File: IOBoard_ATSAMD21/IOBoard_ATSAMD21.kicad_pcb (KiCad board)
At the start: 2 copper layers, 76.2 x 128.5 mm, 36 parts, among them J1 Conn_PIC_ICSP_ICD, J2 Conn_01x04_Male, SW1 EG_1218, SW2 EG_1218, SW3 EG_1218, SW4 EG_1218, U1 ATSAMD21G18A-A, U2 AP2112K-3.3

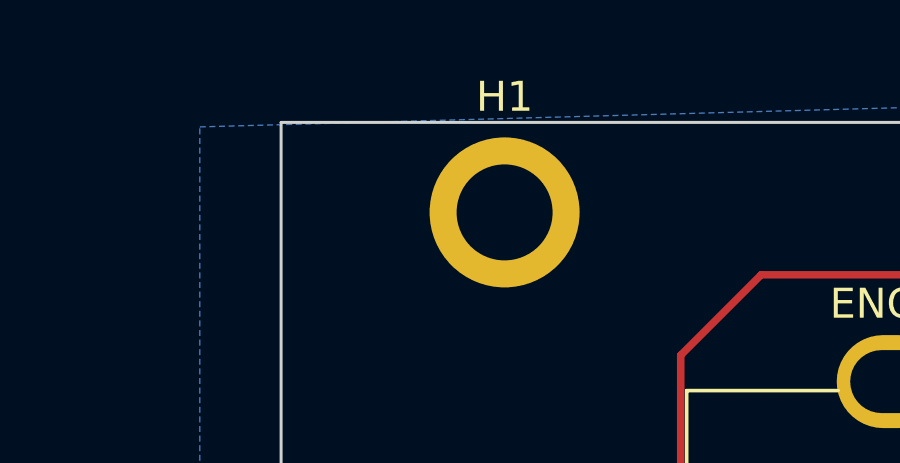
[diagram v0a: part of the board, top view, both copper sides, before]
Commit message: added dimensions to f.fab layer
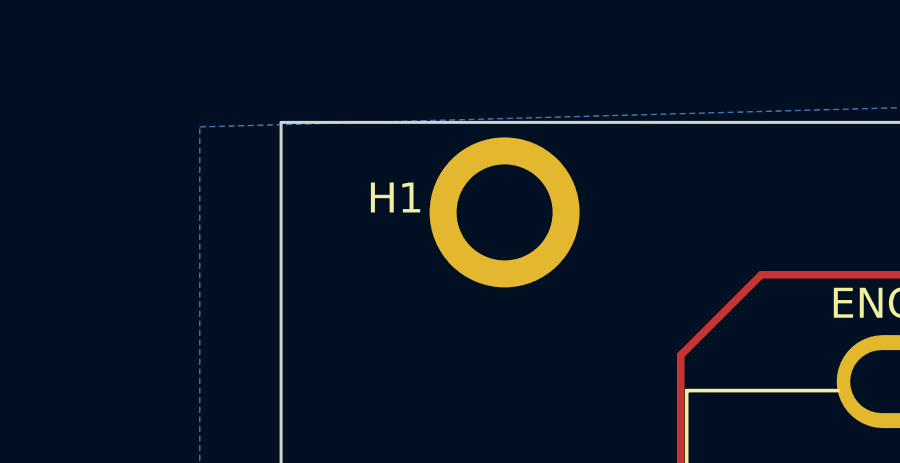
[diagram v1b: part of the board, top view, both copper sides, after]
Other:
- board text added: "0.6in"
- board text added: "0.8in"
- board text added: "1.4in"
- board text added: "1in"
- board text added: "3mm"
- board text added: "7.45mm"
- board text added: "Board Height: 128.5mm/5.06in"
- board text added: "Board Width: 76.2mm/3in/15HP"
- board text added: "Distance from left to right holes: 60.96mm/2.6in/13HP"
- board text added: "LEDs from top: 4.35in"
- board text added: "Switches from top: 3.6in"
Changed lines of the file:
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@@
     )
     (pad_to_mask_clearance 0)
-    (grid_origin 57.45 50)
+    (grid_origin 50 50)
     (pcbplotparams
       (layerselection 0x00010fc_ffffffff)
@@
       (effects (font (size 1 1) (thickness 0.15)))
     )
-    (fp_text value "RotaryEncoder_Switch" (at 1.92 11.12 180 unlocked) (layer "F.Fab")
+    (fp_text value "RotaryEncoder_Switch" (at -0.46 -10.16 unlocked) (layer "F.Fab")
       (effects (font (size 1 1) (thickness 0.15)))
     )
     (fp_text user "${REFERENCE}" (at -0.36 0 270) (layer "F.Fab")
-      (effects (font (size 1 1) (thickness 0.15)))
-    )
-    (fp_text user "${REFERENCE}" (at 1.46 12.62 180 unlocked) (layer "F.Fab")
       (effects (font (size 1 1) (thickness 0.15)))
     )
@@
     (property "Sheetname" "")
     (attr exclude_from_pos_files)
-    (fp_text reference "H1" (at 0 -3.85) (layer "F.SilkS")
+    (fp_text reference "H1" (at -3.64 -0.46) (layer "F.SilkS")
       (effects (font (size 1 1) (thickness 0.15)))
     )
@@
   )
   (gr_rect (start 50 50) (end 126.2 178.5) (layer "Edge.Cuts") (width 0.1) (fill none))
+  (gr_line (start 126.2 43.65) (end 126.2 42.38) (layer "B.Fab") (width 0.1))
+  (gr_line (start 136.36 178.27) (end 135.09 178.27) (layer "B.Fab") (width 0.1))
+  (gr_line (start 137.63 50) (end 136.36 50) (layer "B.Fab") (width 0.1))
+  (gr_line (start 50 43.65) (end 50 42.38) (layer "B.Fab") (width 0.1))
+  (gr_line (start 95.72 160.49) (end 110.96 160.49) (layer "F.Fab") (width 0.1))
+  (gr_line (start 118.58 47.46) (end 118.58 46.19) (layer "F.Fab") (width 0.1))
+  (gr_line (start 118.58 46.19) (end 118.58 47.46) (layer "F.Fab") (width 0.1))
+  (gr_line (start 70.32 65.24) (end 50 65.24) (layer "F.Fab") (width 0.1))
+  (gr_line (start 114.77 160.49) (end 110.96 160.49) (layer "F.Fab") (width 0.1))
+  (gr_line (start 110.96 160.49) (end 126.2 160.49) (layer "F.Fab") (width 0.1))
+  (gr_line (start 70.32 90.64) (end 71.59 90.64) (layer "F.Fab") (width 0.1))
+  (gr_line (start 65.24 141.44) (end 50 141.44) (layer "F.Fab") (width 0.1))
+  (gr_line (start 50 46.19) (end 50 47.46) (layer "F.Fab") (width 0.1))
+  (gr_line (start 46 50) (end 47 50) (layer "F.Fab") (width 0.1))
+  (gr_line (start 135.09 178.27) (end 137.63 178.27) (layer "F.Fab") (width 0.1))
+  (gr_line (start 57.62 47.46) (end 57.62 48.73) (layer "F.Fab") (width 0.1))
+  (gr_line (start 80.48 160.49) (end 95.72 160.49) (layer "F.Fab") (width 0.1))
+  (gr_line (start 132.55 50) (end 132.55 160.49) (layer "F.Fab") (width 0.1))
+  (gr_line (start 110.96 141.44) (end 95.72 141.44) (layer "F.Fab") (width 0.1))
+  (gr_line (start 46 53) (end 48 53) (layer "F.Fab") (width 0.1))
+  (gr_line (start 47 50) (end 47 53) (layer "F.Fab") (width 0.1))
+  (gr_line (start 118.58 47.46) (end 57.62 47.46) (layer "F.Fab") (width 0.1))
+  (gr_line (start 130.01 141.44) (end 127.47 141.44) (layer "F.Fab") (width 0.1))
+  (gr_line (start 105.88 50) (end 105.88 65.24) (layer "F.Fab") (width 0.1))
+  (gr_line (start 70.32 90.64) (end 69.05 90.64) (layer "F.Fab") (width 0.1))
+  (gr_line (start 50 43.65) (end 126.2 43.65) (layer "F.Fab") (width 0.1))
+  (gr_line (start 131.28 160.49) (end 133.82 160.49) (layer "F.Fab") (width 0.1))
+  (gr_line (start 70.32 65.24) (end 70.32 66.51) (layer "F.Fab") (width 0.1))
+  (gr_line (start 50 48.73) (end 50 47.46) (layer "F.Fab") (width 0.1))
+  (gr_line (start 70.32 65.24) (end 70.32 63.97) (layer "F.Fab") (width 0.1))
+  (gr_line (start 127.47 141.44) (end 128.74 141.44) (layer "F.Fab") (width 0.1))
+  (gr_line (start 95.72 141.44) (end 110.96 141.44) (layer "F.Fab") (width 0.1))
+  (gr_line (start 132.55 160.49) (end 131.28 160.49) (layer "F.Fab") (width 0.1))
+  (gr_line (start 105.88 65.24) (end 70.32 65.24) (layer "F.Fab") (width 0.1))
+  (gr_line (start 48 50) (end 46 50) (layer "F.Fab") (width 0.1))
+  (gr_line (start 65.24 141.44) (end 80.48 141.44) (layer "F.Fab") (width 0.1))
+  (gr_line (start 65.24 160.61) (end 80.48 160.49) (layer "F.Fab") (width 0.1))
+  (gr_line (start 80.48 141.44) (end 95.72 141.44) (layer "F.Fab") (width 0.1))
+  (gr_line (start 110.96 141.44) (end 126.2 141.44) (layer "F.Fab") (width 0.1))
+  (gr_line (start 48 53) (end 47 53) (layer "F.Fab") (width 0.1))
+  (gr_line (start 70.32 63.97) (end 70.32 65.24) (layer "F.Fab") (width 0.1))
+  (gr_line (start 118.58 48.73) (end 118.58 47.46) (layer "F.Fab") (width 0.1))
+  (gr_line (start 127.47 50) (end 130.01 50) (layer "F.Fab") (width 0.1))
+  (gr_line (start 70.32 90.64) (end 70.32 65.24) (layer "F.Fab") (width 0.1))
+  (gr_line locked (start 128.74 141.44) (end 128.74 50) (layer "F.Fab") (width 0.1))
+  (gr_line (start 126.2 42.38) (end 126.2 44.92) (layer "F.Fab") (width 0.1))
+  (gr_line (start 133.82 50) (end 131.28 50) (layer "F.Fab") (width 0.1))
+  (gr_line (start 57.62 47.46) (end 50 47.46) (layer "F.Fab") (width 0.1))
+  (gr_line (start 57.62 47.46) (end 57.62 46.19) (layer "F.Fab") (width 0.1))
+  (gr_line (start 69.05 90.64) (end 70.32 90.64) (layer "F.Fab") (width 0.1))
+  (gr_line (start 135.09 50) (end 137.63 50) (layer "F.Fab") (width 0.1))
+  (gr_line (start 47 53) (end 46 53) (layer "F.Fab") (width 0.1))
+  (gr_line (start 136.36 50) (end 136.36 178.27) (layer "F.Fab") (width 0.1))
+  (gr_line (start 50 47.46) (end 50 46.19) (layer "F.Fab") (width 0.1))
+  (gr_line (start 50 42.38) (end 50 44.92) (layer "F.Fab") (width 0.1))
   (gr_text "MCLR" (at 58.466 113.452) (layer "F.SilkS")
     (effects (font (size 1 1) (thickness 0.15)))
@@
     (effects (font (size 1 1) (thickness 0.15)))
   )
+  (gr_text "0.6in\n" (at 103.34 159.22) (layer "F.Fab")
+    (effects (font (size 1 1) (thickness 0.15)))
+  )
+  (gr_text "0.6in\n" (at 86.83 159.22) (layer "F.Fab")
+    (effects (font (size 1 1) (thickness 0.15)))
+  )
+  (gr_text "Switches from top: 3.6in" (at 130.01 100.8 270) (layer "F.Fab")
+    (effects (font (size 1 1) (thickness 0.15)))
+  )
+  (gr_text "0.6in\n" (at 72.86 159.22) (layer "F.Fab")
+    (effects (font (size 1 1) (thickness 0.15)))
+  )
+  (gr_text "0.6in" (at 89.37 140.17) (layer "F.Fab")
+    (effects (font (size 1 1) (thickness 0.15)))
+  )
+  (gr_text "0.8in" (at 107.15 59.04 90) (layer "F.Fab")
+    (effects (font (size 1 1) (thickness 0.15)))
+  )
+  (gr_text "3mm" (at 43.65 51.27) (layer "F.Fab")
+    (effects (font (size 1 1) (thickness 0.15)))
+  )
+  (gr_text "0.6in" (at 118.58 140.17) (layer "F.Fab")
+    (effects (font (size 1 1) (thickness 0.15)))
+  )
+  (gr_text "1.4in" (at 88.1 63.97) (layer "F.Fab")
+    (effects (font (size 1 1) (thickness 0.15)))
+  )
+  (gr_text "Board Height: 128.5mm/5.06in" (at 137.63 99.53 270) (layer "F.Fab")
+    (effects (font (size 1 1) (thickness 0.15)))
+  )
+  (gr_text "0.6in\n" (at 104.61 140.17) (layer "F.Fab")
+    (effects (font (size 1 1) (thickness 0.15)))
+  )
+  (gr_text "7.45mm" (at 53.81 46.19) (layer "F.Fab")
+    (effects (font (size 1 1) (thickness 0.15)))
+  )
+  (gr_text "0.8in" (at 58.89 63.97) (layer "F.Fab")
+    (effects (font (size 1 1) (thickness 0.15)))
+  )
+  (gr_text "0.6in\n" (at 118.58 159.22) (layer "F.Fab")
+    (effects (font (size 1 1) (thickness 0.15)))
+  )
+  (gr_text "LEDs from top: 4.35in\n" (at 133.82 100.8 270) (layer "F.Fab")
+    (effects (font (size 1 1) (thickness 0.15)))
+  )
+  (gr_text "0.6in\n" (at 58.89 140.17) (layer "F.Fab")
+    (effects (font (size 1 1) (thickness 0.15)))
+  )
+  (gr_text "Distance from left to right holes: 60.96mm/2.6in/13HP" (at 89.37 46.19) (layer "F.Fab")
+    (effects (font (size 1 1) (thickness 0.15)))
+  )
+  (gr_text "Board Width: 76.2mm/3in/15HP\n" (at 88.1 42.38) (layer "F.Fab")
+    (effects (font (size 1 1) (thickness 0.15)))
+  )
+  (gr_text "0.6in\n" (at 72.86 140.17) (layer "F.Fab")
+    (effects (font (size 1 1) (thickness 0.15)))
+  )
+  (gr_text "1in" (at 69.05 75.4 90) (layer "F.Fab")
+    (effects (font (size 1 1) (thickness 0.15)))
+  )

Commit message: IOBoard v3 WIP
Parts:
- removed J2: Conn_01x04_Male, Connector_PinHeader_2.54mm:PinHeader_1x04_P2.54mm_Vertical
- added C12: 10uF, Capacitor_SMD:C_0603_1608Metric, F.Cu at (186.0, 26.3)
- added C13: 10nF, Capacitor_SMD:C_0603_1608Metric, F.Cu at (186.0, 28.8)
- added C14: 10uF, Capacitor_SMD:C_0603_1608Metric, F.Cu at (186.0, 31.3)
- added C15: 10uF, Capacitor_SMD:C_0603_1608Metric, F.Cu at (186.0, 33.8)
- added C16: 10nF, Capacitor_SMD:C_0603_1608Metric, F.Cu at (186.0, 36.3)
- added C17: 10uF, Capacitor_SMD:C_0603_1608Metric, F.Cu at (186.0, 38.8)
- added C18: 10uF, Capacitor_SMD:C_0603_1608Metric, F.Cu at (186.0, 41.3)
- added C19: 10uF, Capacitor_SMD:C_0603_1608Metric, F.Cu at (190.0, 26.3)
- added C21: 10uF, Capacitor_SMD:C_0603_1608Metric, F.Cu at (190.0, 28.8)
- added FB1: FerriteBead, Inductor_SMD:L_0603_1608Metric_Pad1.05x0.95mm_HandSolder, F.Cu at (186.2, 56.8)
- added J5: Conn_01x03_Pin, Connector_PinHeader_2.54mm:PinHeader_1x03_P2.54mm_Vertical, F.Cu at (121.9, 109.7)
- added J6: Conn_02x03_Odd_Even, Connector_PinHeader_2.54mm:PinHeader_2x03_P2.54mm_Vertical, F.Cu at (194.8, 44.9)
- added J9: Conn_01x03_Pin, Connector_PinHeader_2.54mm:PinHeader_1x03_P2.54mm_Vertical, F.Cu at (121.9, 98.6)
- added R10: 100, Resistor_SMD:R_0603_1608Metric, F.Cu at (190.0, 41.3)
- added R11: 100, Resistor_SMD:R_0603_1608Metric, F.Cu at (194.0, 26.3)
- added R12: 1000, Resistor_SMD:R_0603_1608Metric, F.Cu at (194.0, 28.8)
- added R13: 100, Resistor_SMD:R_0603_1608Metric, F.Cu at (194.0, 31.3)
- added R14: 470, Resistor_SMD:R_0603_1608Metric, F.Cu at (194.0, 33.8)
- added R15: 100, Resistor_SMD:R_0603_1608Metric, F.Cu at (194.0, 36.3)
- added R17: 1000, Resistor_SMD:R_0603_1608Metric, F.Cu at (194.0, 38.8)
- added R18: 100, Resistor_SMD:R_0603_1608Metric, F.Cu at (194.0, 41.3)
- added R6: 100, Resistor_SMD:R_0603_1608Metric, F.Cu at (190.0, 31.3)
- added R7: 10, Resistor_SMD:R_0603_1608Metric, F.Cu at (190.0, 33.8)
- added R8: 100, Resistor_SMD:R_0603_1608Metric, F.Cu at (190.0, 36.3)
- added R9: 1000, Resistor_SMD:R_0603_1608Metric, F.Cu at (190.0, 38.8)
- added S1: EG1218, customlib:EG_1218, F.Cu at (177.7, 25.8)
- added S2: EG1218, customlib:EG_1218, F.Cu at (177.7, 34.0)
- added S3: EG1218, customlib:EG_1218, F.Cu at (177.7, 42.3)
- added U3: LM2904, Package_SO:SOIC-8_3.9x4.9mm_P1.27mm, F.Cu at (188.2, 45.8)
- added U9: LM2904, Package_SO:SOIC-8_3.9x4.9mm_P1.27mm, F.Cu at (188.2, 52.3)
- ENC0, ENC1, ENC2, ENC3: footprint custom_lib:PEC12R-3217F-S0024-ND -> customlib:PEC12R-3217F-S0024-ND
- SW1, SW2, SW3, SW4: footprint custom_lib:EG_1218 -> customlib:EG_1218
- moved H3 230.4 mm to (246.0, 43.0)
- moved H1 190.1 mm to (246.0, 28.5)
- moved H4 178.8 mm to (246.0, 50.3)
- moved H2 128.7 mm to (246.0, 35.8)
- moved C6 38.1 mm to (87.6, 87.0), turned to -90 degrees
- moved C1 37.5 mm to (81.3, 77.0), turned to 0 degrees
- moved U1 37.5 mm to (88.1, 78.6)
- moved C3 37.3 mm to (94.0, 79.0)
- moved C4 37.1 mm to (95.5, 79.0)
- moved R1 36.6 mm to (65.2, 130.2)
- moved R2 36.6 mm to (80.5, 130.2)
- moved R3 36.6 mm to (95.7, 130.2)
- moved R4 36.6 mm to (111.0, 130.2)
- moved C8 36.5 mm to (81.8, 72.5), turned to 0 degrees
- moved C9 36.5 mm to (81.8, 74.0), turned to 180 degrees
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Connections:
- C1 pad 1: GND -> GNDD
- C10 pad 2: GND -> GNDD
- C11 pad 1: GND -> GNDD
- C2 pad 1: GND -> GNDD
- C3 pad 2: GND -> GNDD
- C4 pad 1: GND -> GNDD
- C5 pad 2: GND -> GNDD
- C6 pad 2: GND -> GNDD
- C7 pad 1: GND -> GNDD
- C8 pad 2: GND -> GNDD
- C9 pad 1: GND -> GNDD
- ENC0 pad C: GND -> GNDA
- ENC1 pad C: GND -> GNDA
- ENC2 pad C: GND -> GNDA
- ENC3 pad C: GND -> GNDA
- H1 pad 1: GND -> GNDD
- H2 pad 1: GND -> GNDD
- H3 pad 1: GND -> GNDA
- H4 pad 1: GND -> GNDA
- J1 pad 3: GND -> GNDD
- J1 pad 4: /SWDIO -> /SWCLK
- J1 pad 5: /SWCLK -> /SWDIO
- R1 pad 1: GND -> GNDD
- R2 pad 1: GND -> GNDD
- R3 pad 1: GND -> GNDD
- R4 pad 1: GND -> GNDD
- U1 pad 18: GND -> GNDD
- U1 pad 35: GND -> GNDD
- U1 pad 42: GND -> GNDD
- U1 pad 5: GND -> GNDD
- U2 pad 2: GND -> GNDD
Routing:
- net /ENC1_SW: track 80.7 -> 32.0 mm
- net GNDD: track 0.00 -> 43.8 mm, vias 0 -> 9
- net GND: track 43.2 -> 0.00 mm, vias 10 -> 0
- net /ENC2_A: track 52.9 -> 13.2 mm
- net /ENC1_B: track 53.5 -> 15.6 mm
- net /ENC2_B: track 47.7 -> 10.5 mm
- net /ENC2_SW: track 60.6 -> 24.4 mm
- net /ENC1_A: track 48.3 -> 13.6 mm
- net /ENC0_SW: track 55.9 -> 35.7 mm
- net /SCL: track 30.3 -> 44.8 mm
- net /SDA: track 31.2 -> 45.2 mm
- net /SWCLK: track 31.5 -> 45.2 mm
- net /ENC0_A: track 22.3 -> 33.7 mm
- net VCC: track 18.4 -> 8.20 mm
- net /ENC3_A: track 26.9 -> 17.4 mm
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- added copper zone on F.Cu, net GNDD
- added copper zone on F.Cu, net VCC
- removed copper zone on B.Cu, net GND
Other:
- board size 76.2 x 128.5 mm -> 76.2 x 112 mm
- board text added: "ADC_In"
- board text added: "C8"
- board text added: "GNDA"
- board text added: "GNDD"
- board text added: "I2C/ADC"
- board text added: "IO Board - ATSAMD21G18AU V3 Bloom 5/19/23"
- board text added: "Power"
- board text added: "Programming Header"
- board text added: "VDD"
- board text removed: "0.6in"
- board text removed: "0.8in"
- board text removed: "1.4in"
- board text removed: "1in"
- board text removed: "3mm"
- board text removed: "IO Board - ATSAMD21G18AU V2 Bloom 3/30/23"

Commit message: IO Board v3
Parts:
- removed H1, H2, H3, H4: MountingHole_Pad, MountingHole:MountingHole_3.2mm_M3_ISO7380_Pad
- removed J9: Conn_01x03_Pin, Connector_PinHeader_2.54mm:PinHeader_1x03_P2.54mm_Vertical
- added J10: Eurorack_Mono_Jack, winterbloom:AudioJack_WQP518MA, F.Cu at (116.0, 162.4)
- added J11: Conn_01x04_Pin, Connector_PinHeader_2.54mm:PinHeader_1x04_P2.54mm_Vertical, F.Cu at (121.9, 96.9)
- added J2: Eurorack_Mono_Jack, winterbloom:AudioJack_WQP518MA, F.Cu at (116.0, 142.1)
- added J3: Eurorack_Mono_Jack, winterbloom:AudioJack_WQP518MA, F.Cu at (88.1, 142.1)
- added J4: Eurorack_Mono_Jack, winterbloom:AudioJack_WQP518MA, F.Cu at (88.1, 162.4)
- added J7: Eurorack_Mono_Jack, winterbloom:AudioJack_WQP518MA, F.Cu at (60.2, 142.1)
- added J8: Eurorack_Mono_Jack, winterbloom:AudioJack_WQP518MA, F.Cu at (60.2, 162.4)
- FB1: moved to B.Cu
- moved R11 184.2 mm to (71.8, 164.1), turned to 90 degrees
- moved R13 182.7 mm to (71.8, 167.2), turned to 90 degrees
- moved R12 177.1 mm to (71.3, 156.5), turned to -90 degrees
- moved C15 174.3 mm to (67.5, 161.6), turned to -90 degrees
- moved R8 174.2 mm to (69.1, 161.6), turned to 90 degrees
- moved R14 172.9 mm to (77.1, 161.1), turned to -90 degrees
- moved C16 170.4 mm to (73.4, 164.2), turned to 90 degrees
- moved C17 164.8 mm to (75.5, 161.1), turned to -90 degrees
- moved S2 164.3 mm to (62.2, 151.0), turned to 90 degrees
- moved C18 164.1 mm to (73.9, 161.1), turned to -90 degrees
- moved S1 161.2 mm to (76.2, 151.0), turned to 90 degrees
- moved R9 158.7 mm to (72.6, 145.6), turned to 90 degrees
- moved C13 157.8 mm to (75.4, 141.3), turned to -90 degrees
- moved C14 157.1 mm to (76.9, 144.3), turned to 90 degrees
- moved R6 156.7 mm to (78.4, 141.3), turned to -90 degrees
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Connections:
- ENC0 pad C: GNDA -> GNDD
- ENC1 pad C: GNDA -> GNDD
- ENC2 pad C: GNDA -> GNDD
- ENC3 pad C: GNDA -> GNDD
- U3 pad 4: GNDD -> GNDA
- U9 pad 4: GNDD -> GNDA
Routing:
- net /DAC_out: track 0.00 -> 83.2 mm, vias 0 -> 1
- net /ADC_in: track 0.00 -> 80.6 mm
- net /CV_out: track 0.00 -> 77.0 mm
- net /Audio_out: track 0.00 -> 68.4 mm
- net /LL_out: track 0.00 -> 64.6 mm
- net VCC: track 8.20 -> 64.1 mm, vias 0 -> 1
- net /CV_in: track 0.00 -> 42.1 mm
- net +3.3V: track 14.5 -> 52.3 mm, vias 0 -> 12
- net Net-(U9B--): track 0.00 -> 25.5 mm
- net GNDA: track 0.00 -> 24.7 mm, vias 0 -> 4
- net /LL_in: track 0.00 -> 24.2 mm
- net Net-(U9A--): track 0.00 -> 20.2 mm
- net Net-(J7-Tip): track 0.00 -> 14.3 mm
- net Net-(J3-Tip): track 0.00 -> 14.3 mm
- net Net-(U3A--): track 0.00 -> 12.0 mm
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- added copper zone on B.Cu, net GNDA
- added copper zone on B.Cu, net GNDD
- removed copper zone on F.Cu, net VCC
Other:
- board text added: "Audio_out"
- board text added: "CV"
- board text added: "CV1"
- board text added: "CV2"
- board text added: "CV_in"
- board text added: "CV_out"
- board text added: "Control Voltage"
- board text added: "DAC_out"
- board text added: "IO Board - ATSAMD21 V3 Bloom 5/19/23"
- board text added: "IO Board V3"
- board text added: "Input/Output Jumpers"
- board text added: "LL"
- board text added: "LL1"
- board text added: "LL2"
- board text added: "LL_in"
- board text added: "LL_out"
- board text added: "Line Level"
- board text removed: "7.45mm"
- board text removed: "Board Height: 128.5mm/5.06in"
- board text removed: "Board Width: 76.2mm/3in/15HP"
- board text removed: "Distance from left to right holes: 60.96mm/2.6in/13HP"
- board text removed: "IO Board - ATSAMD21G18AU V3 Bloom 5/19/23"
- board text removed: "LEDs from top: 4.35in"
- board text removed: "Switches from top: 3.6in"

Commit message: changing io
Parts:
- moved C21 7.60 mm to (103.3, 156.9), turned to -90 degrees
- moved R17 7.14 mm to (107.4, 156.7), turned to -90 degrees
- moved R18 6.92 mm to (105.4, 156.9), turned to -90 degrees
- moved C7 2.51 mm to (87.3, 88.7), turned to 0 degrees
- moved U3 2.47 mm to (105.9, 150.3), turned to 90 degrees
- moved C4 0.85 mm to (96.4, 79.0)
- moved C10 0.59 mm to (80.5, 82.4)
- moved C3 0.47 mm to (94.5, 79.0)
- moved C6 0.30 mm to (87.3, 86.8), turned to 180 degrees
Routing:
- net /Audio_out: track 68.4 -> 53.5 mm
- net Net-(U3A--): track 12.0 -> 22.2 mm
- net VCC: track 64.1 -> 54.1 mm
- net /CV_out: track 77.0 -> 85.1 mm
- net GNDA: track 24.7 -> 19.3 mm, vias 4 -> 5
- net +3.3V: track 52.3 -> 48.7 mm
- net /ADC_in: track 80.6 -> 77.2 mm
- net GNDD: track 51.6 -> 54.5 mm, vias 11 -> 12
- net Net-(J1-~{MCLR}/VPP): track 2.63 -> 5.26 mm
- net /ENC3_A: track 17.4 -> 18.0 mm
- net /ENC3_B: track 20.6 -> 21.2 mm
- net /ENC3_SW: track 40.5 -> 41.0 mm

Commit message: added IO Board dimensions
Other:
- board text added: "8.25 mm off top and bottom of front plate :)"
